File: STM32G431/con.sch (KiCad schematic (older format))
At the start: 61 parts, among them J10 NTC, J11 LED, J4 GND, J5 VIN, J6 UART, J8 HALL, J9 AIN/PWM, P1 TC2030-CTX-Tag-Connect, Q2 Q_NMOS_GSD, U11 USBLC6-4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

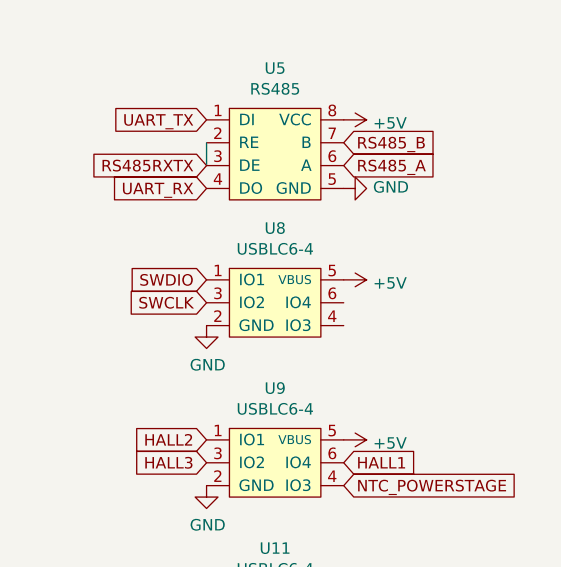
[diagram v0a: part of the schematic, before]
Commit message: updated layout
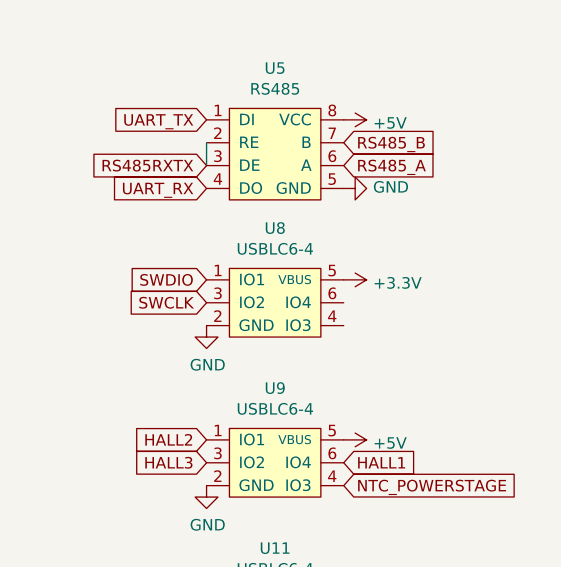
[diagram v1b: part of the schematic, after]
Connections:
- net +3V3: now also U8.5 (VBUS)
- net +5V: no longer U8.5 (VBUS)
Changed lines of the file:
@@
-	0    1    1    0
-$EndComp
-$Comp
-L power:+5V #PWR0171
-U 1 1 5CEAAB05
-P 10150 3400
-F 0 "#PWR0171" H 10150 3250 50  0001 C CNN
-F 1 "+5V" V 10165 3528 50  0000 L CNN
-F 2 "" H 10150 3400 50  0001 C CNN
-F 3 "" H 10150 3400 50  0001 C CNN
-	1    10150 3400
 	0    1    1    0
 $EndComp
@@
 Text Label 7650 1100 0    50   ~ 0
 AinC
+$Comp
+L power:+3.3V #PWR?
+U 1 1 5E15C1C9
+P 10150 3400
+F 0 "#PWR?" H 10150 3250 50  0001 C CNN
+F 1 "+3.3V" V 10165 3528 50  0000 L CNN
+F 2 "" H 10150 3400 50  0001 C CNN
+F 3 "" H 10150 3400 50  0001 C CNN
+	1    10150 3400
+	0    1    1    0
+$EndComp
 $EndSCHEMATC

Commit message: updated layout
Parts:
- R27, R28, R29, R33, R34, R35: footprint Resistor_SMD:R_0402_1005Metric -> Resistor_SMD:R_0603_1608Metric
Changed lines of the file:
@@
 F 0 "R35" H 6458 1704 50  0000 L CNN
 F 1 "10k" H 6458 1795 50  0000 L CNN
-F 2 "Resistor_SMD:R_0402_1005Metric" H 6400 1750 50  0001 C CNN
+F 2 "Resistor_SMD:R_0603_1608Metric" H 6400 1750 50  0001 C CNN
 F 3 "~" H 6400 1750 50  0001 C CNN
 	1    6400 1750
@@
 F 0 "R34" H 6600 2100 50  0000 R CNN
 F 1 "10k" H 6550 1950 50  0000 R CNN
-F 2 "Resistor_SMD:R_0402_1005Metric" H 6500 1750 50  0001 C CNN
+F 2 "Resistor_SMD:R_0603_1608Metric" H 6500 1750 50  0001 C CNN
 F 3 "~" H 6500 1750 50  0001 C CNN
 	1    6500 1750
@@
 F 0 "R33" H 6541 1704 50  0000 R CNN
 F 1 "10k" H 6541 1795 50  0000 R CNN
-F 2 "Resistor_SMD:R_0402_1005Metric" H 6600 1750 50  0001 C CNN
+F 2 "Resistor_SMD:R_0603_1608Metric" H 6600 1750 50  0001 C CNN
 F 3 "~" H 6600 1750 50  0001 C CNN
 	1    6600 1750
@@
 F 0 "R28" V 6200 750 50  0000 C CNN
 F 1 "1.8k" V 6300 750 50  0000 C CNN
-F 2 "Resistor_SMD:R_0402_1005Metric" H 6250 1200 50  0001 C CNN
+F 2 "Resistor_SMD:R_0603_1608Metric" H 6250 1200 50  0001 C CNN
 F 3 "~" H 6250 1200 50  0001 C CNN
 	1    6250 1200
@@
 F 0 "R27" V 6054 1100 50  0000 C CNN
 F 1 "1.8k" V 6145 1100 50  0000 C CNN
-F 2 "Resistor_SMD:R_0402_1005Metric" H 6250 1100 50  0001 C CNN
+F 2 "Resistor_SMD:R_0603_1608Metric" H 6250 1100 50  0001 C CNN
 F 3 "~" H 6250 1100 50  0001 C CNN
 	1    6250 1100
@@
 F 0 "R29" V 6354 1300 50  0000 C CNN
 F 1 "1.8k" V 6445 1300 50  0000 C CNN
-F 2 "Resistor_SMD:R_0402_1005Metric" H 6250 1300 50  0001 C CNN
+F 2 "Resistor_SMD:R_0603_1608Metric" H 6250 1300 50  0001 C CNN
 F 3 "~" H 6250 1300 50  0001 C CNN
 	1    6250 1300

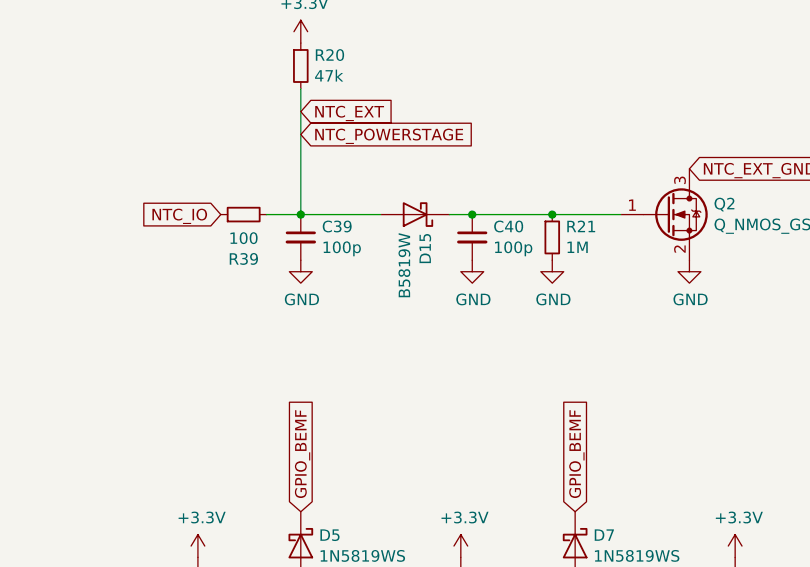
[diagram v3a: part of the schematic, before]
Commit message: updated layout
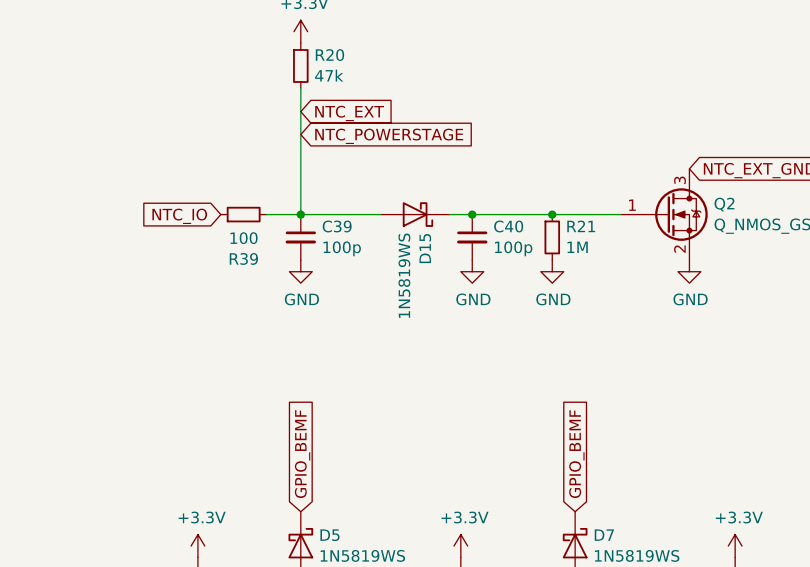
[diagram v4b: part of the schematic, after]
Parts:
- D15: value B5819W -> 1N5819WS; footprint Diode_SMD:D_SOD-123 -> Diode_SMD:D_SOD-323
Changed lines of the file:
@@
 P 4650 5200
 F 0 "D15" V 4604 5279 50  0000 L CNN
-F 1 "B5819W" V 4695 5279 50  0000 L CNN
-F 2 "Diode_SMD:D_SOD-123" H 4650 5200 50  0001 C CNN
+F 1 "1N5819WS" V 4695 5279 50  0000 L CNN
+F 2 "Diode_SMD:D_SOD-323" H 4650 5200 50  0001 C CNN
 F 3 "https://datasheet.lcsc.com/szlcsc/Changjiang-Electronics-Tech-CJ-B5819W_C8598.pdf" H 4650 5200 50  0001 C CNN
 F 4 "C8598" H 4650 5200 50  0001 C CNN "LCSC"

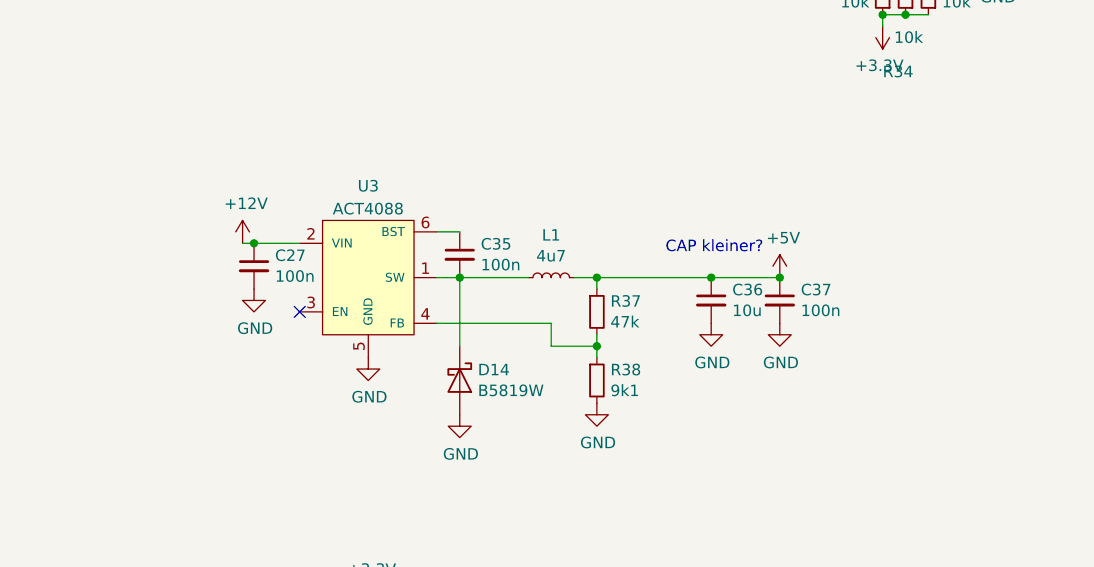
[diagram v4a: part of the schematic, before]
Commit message: updated layout
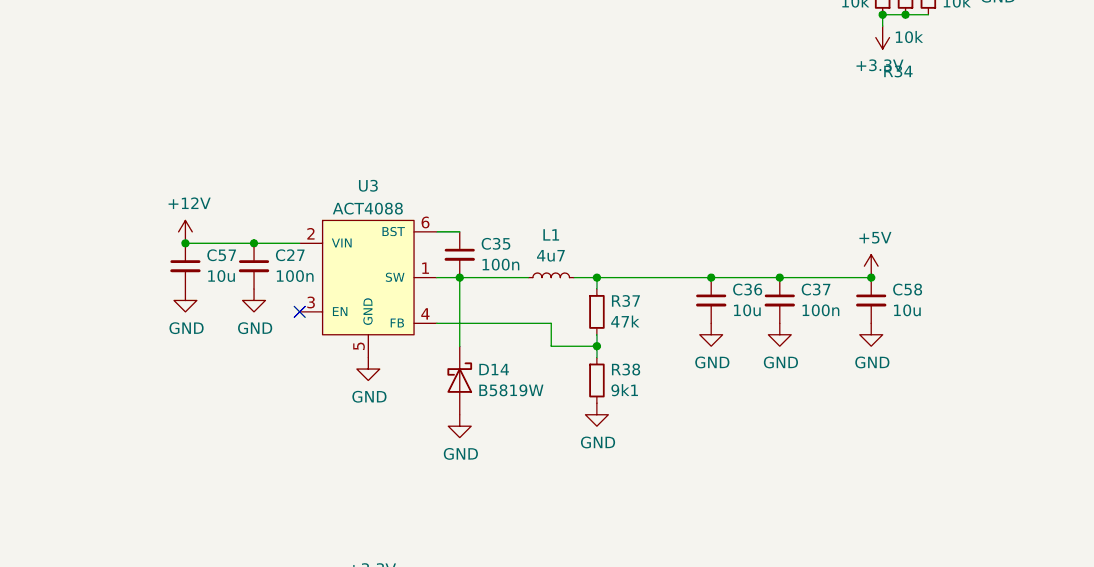
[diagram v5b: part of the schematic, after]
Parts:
- added C57, C58: 10u, Capacitor_SMD:C_1206_3216Metric, symbol Device:C_Small
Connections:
- net +12V: now also C57.1
- net +5V: now also C58.1
- net GND: now also C57.2, C58.2
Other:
- note removed: "CAP kleiner?"
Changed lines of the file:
@@
 L power:+5V #PWR0150
 U 1 1 5CEAAA14
-P 5950 3000
-F 0 "#PWR0150" H 5950 2850 50  0001 C CNN
-F 1 "+5V" H 5965 3173 50  0000 C CNN
-F 2 "" H 5950 3000 50  0001 C CNN
-F 3 "" H 5950 3000 50  0001 C CNN
-	1    5950 3000
+P 6350 3000
+F 0 "#PWR0150" H 6350 2850 50  0001 C CNN
+F 1 "+5V" H 6365 3173 50  0000 C CNN
+F 2 "" H 6350 3000 50  0001 C CNN
+F 3 "" H 6350 3000 50  0001 C CNN
+	1    6350 3000
 	1    0    0    -1
 $EndComp
@@
 	3650 2850 3850 2850
 Connection ~ 3650 2850
-Wire Wire Line
-	3600 2850 3650 2850
 $Comp
 L Device:C_Small C27
@@
 	1    0    0    -1
 $EndComp
-Text Notes 5450 2900 0    50   ~ 0
-CAP kleiner?
 Text GLabel 2750 7150 2    50   Input ~ 0
 SWCLK
@@
 L power:+12V #PWR0217
 U 1 1 5DED744B
-P 3600 2850
-F 0 "#PWR0217" H 3600 2700 50  0001 C CNN
-F 1 "+12V" H 3615 3023 50  0000 C CNN
-F 2 "" H 3600 2850 50  0001 C CNN
-F 3 "" H 3600 2850 50  0001 C CNN
-	1    3600 2850
+P 3350 2850
+F 0 "#PWR0217" H 3350 2700 50  0001 C CNN
+F 1 "+12V" H 3365 3023 50  0000 C CNN
+F 2 "" H 3350 2850 50  0001 C CNN
+F 3 "" H 3350 2850 50  0001 C CNN
+	1    3350 2850
 	1    0    0    -1
 $EndComp
@@
 	0    1    1    0
 $EndComp
+$Comp
+L power:GND #PWR0234
+U 1 1 5DF96379
+P 6350 3200
+F 0 "#PWR0234" H 6350 2950 50  0001 C CNN
+F 1 "GND" H 6355 3027 50  0000 C CNN
+F 2 "" H 6350 3200 50  0001 C CNN
+F 3 "" H 6350 3200 50  0001 C CNN
+	1    6350 3200
+	1    0    0    -1
+$EndComp
+$Comp
+L Device:C_Small C58
+U 1 1 5DF9637F
+P 6350 3100
+F 0 "C58" H 6442 3146 50  0000 L CNN
+F 1 "10u" H 6442 3055 50  0000 L CNN
+F 2 "Capacitor_SMD:C_1206_3216Metric" H 6350 3100 50  0001 C CNN
+F 3 "~" H 6350 3100 50  0001 C CNN
+	1    6350 3100
+	1    0    0    -1
+$EndComp
+$Comp
+L power:GND #PWR0235
+U 1 1 5DF98EE3
+P 3350 3050
+F 0 "#PWR0235" H 3350 2800 50  0001 C CNN
+F 1 "GND" H 3355 2877 50  0000 C CNN
+F 2 "" H 3350 3050 50  0001 C CNN
+F 3 "" H 3350 3050 50  0001 C CNN
+	1    3350 3050
+	1    0    0    -1
+$EndComp
+$Comp
+L Device:C_Small C57
+U 1 1 5DF98EE9
+P 3350 2950
+F 0 "C57" H 3442 2996 50  0000 L CNN
+F 1 "10u" H 3442 2905 50  0000 L CNN
+F 2 "Capacitor_SMD:C_1206_3216Metric" H 3350 2950 50  0001 C CNN
+F 3 "~" H 3350 2950 50  0001 C CNN
+	1    3350 2950
+	1    0    0    -1
+$EndComp
+Wire Wire Line
+	3350 2850 3650 2850
+Connection ~ 3350 2850
+Wire Wire Line
+	6350 3000 5950 3000
+Connection ~ 6350 3000
 $EndSCHEMATC

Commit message: updated layout
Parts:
- R17, R6: footprint Capacitor_SMD:C_0402_1005Metric -> Resistor_SMD:R_0402_1005Metric
- R23, R25, R30: footprint Resistor_SMD:R_0402_1005Metric -> Resistor_SMD:R_0603_1608Metric
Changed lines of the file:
@@
 F 0 "R30" V 6546 7050 50  0000 C CNN
 F 1 "100k" V 6455 7050 50  0000 C CNN
-F 2 "Resistor_SMD:R_0402_1005Metric" H 6650 7050 50  0001 C CNN
+F 2 "Resistor_SMD:R_0603_1608Metric" H 6650 7050 50  0001 C CNN
 F 3 "~" H 6650 7050 50  0001 C CNN
 	1    6650 7050
@@
 F 0 "R25" V 5604 7050 50  0000 C CNN
 F 1 "100k" V 5695 7050 50  0000 C CNN
-F 2 "Resistor_SMD:R_0402_1005Metric" H 5500 7050 50  0001 C CNN
+F 2 "Resistor_SMD:R_0603_1608Metric" H 5500 7050 50  0001 C CNN
 F 3 "~" H 5500 7050 50  0001 C CNN
 	1    5500 7050
@@
 F 0 "R23" V 4404 7050 50  0000 C CNN
 F 1 "100k" V 4495 7050 50  0000 C CNN
-F 2 "Resistor_SMD:R_0402_1005Metric" H 4300 7050 50  0001 C CNN
+F 2 "Resistor_SMD:R_0603_1608Metric" H 4300 7050 50  0001 C CNN
 F 3 "~" H 4300 7050 50  0001 C CNN
 	1    4300 7050
@@
 F 0 "R6" H 7809 5896 50  0000 L CNN
 F 1 "100k" H 7809 5805 50  0000 L CNN
-F 2 "Capacitor_SMD:C_0402_1005Metric" H 7750 5850 50  0001 C CNN
+F 2 "Resistor_SMD:R_0402_1005Metric" H 7750 5850 50  0001 C CNN
 F 3 "~" H 7750 5850 50  0001 C CNN
 	1    7750 5850
@@
 F 0 "R17" H 7809 6196 50  0000 L CNN
 F 1 "4k3" H 7809 6105 50  0000 L CNN
-F 2 "Capacitor_SMD:C_0402_1005Metric" H 7750 6150 50  0001 C CNN
+F 2 "Resistor_SMD:R_0402_1005Metric" H 7750 6150 50  0001 C CNN
 F 3 "~" H 7750 6150 50  0001 C CNN
 	1    7750 6150

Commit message: updated files
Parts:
- C29, C30, C31: value 100p -> DNP
- C39, C40: footprint Resistor_SMD:R_0402_1005Metric -> Capacitor_SMD:C_0402_1005Metric
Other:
- moved on the sheet: C42, R17, R6
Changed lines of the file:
@@
 EESchema Schematic File Version 4
-LIBS:STM32G431-cache
 EELAYER 30 0
 EELAYER END
@@
 AR Path="/5D59ABFE/5D5B749F" Ref="C31"  Part="1"
 F 0 "C31" H 6092 7246 50  0000 L CNN
-F 1 "100p" H 6092 7155 50  0000 L CNN
+F 1 "DNP" H 6092 7155 50  0000 L CNN
 F 2 "Capacitor_SMD:C_0402_1005Metric" H 6000 7200 50  0001 C CNN
 F 3 "~" H 6000 7200 50  0001 C CNN
@@
 AR Path="/5D59ABFE/5D5B74C4" Ref="C30"  Part="1"
 F 0 "C30" H 4892 7246 50  0000 L CNN
-F 1 "100p" H 4892 7155 50  0000 L CNN
+F 1 "DNP" H 4892 7155 50  0000 L CNN
 F 2 "Capacitor_SMD:C_0402_1005Metric" H 4800 7200 50  0001 C CNN
 F 3 "~" H 4800 7200 50  0001 C CNN
@@
 AR Path="/5D59ABFE/5D5B74E9" Ref="C29"  Part="1"
 F 0 "C29" H 3742 7246 50  0000 L CNN
-F 1 "100p" H 3742 7155 50  0000 L CNN
+F 1 "DNP" H 3742 7155 50  0000 L CNN
 F 2 "Capacitor_SMD:C_0402_1005Metric" H 3650 7200 50  0001 C CNN
 F 3 "~" H 3650 7200 50  0001 C CNN
@@
 F 0 "C39" H 4242 5346 50  0000 L CNN
 F 1 "100p" H 4242 5255 50  0000 L CNN
-F 2 "Resistor_SMD:R_0402_1005Metric" H 4150 5300 50  0001 C CNN
+F 2 "Capacitor_SMD:C_0402_1005Metric" H 4150 5300 50  0001 C CNN
 F 3 "~" H 4150 5300 50  0001 C CNN
 	1    4150 5300
@@
 F 0 "C40" H 4992 5346 50  0000 L CNN
 F 1 "100p" H 4992 5255 50  0000 L CNN
-F 2 "Resistor_SMD:R_0402_1005Metric" H 4900 5300 50  0001 C CNN
+F 2 "Capacitor_SMD:C_0402_1005Metric" H 4900 5300 50  0001 C CNN
 F 3 "~" H 4900 5300 50  0001 C CNN
 	1    4900 5300
@@
 Connection ~ 5250 5200
 $Comp
-L Device:Q_NMOS_GSD Q2
-U 1 1 5CDECFF4
-P 5750 5200
-F 0 "Q2" H 5956 5246 50  0000 L CNN
-F 1 "Q_NMOS_GSD" H 5956 5155 50  0000 L CNN
-F 2 "Package_TO_SOT_SMD:SOT-23" H 5950 5300 50  0001 C CNN
-F 3 "~" H 5750 5200 50  0001 C CNN
-	1    5750 5200
-	1    0    0    -1
-$EndComp
-$Comp
 L power:GND #PWR0181
 U 1 1 5CDEE814
@@
 	1    0    0    -1
 $EndComp
-Text GLabel 5850 5000 2    50   Input ~ 0
+Text GLabel 5850 5000 1    50   Input ~ 0
 NTC_EXT_GND
 Text GLabel 8900 1000 0    50   Input ~ 0
@@
 L Device:R_Small R?
 U 1 1 5CEAA519
-P 7750 5850
+P 7850 4050
 AR Path="/5CEAA519" Ref="R?"  Part="1"
 AR Path="/5D59ABFE/5CEAA519" Ref="R6"  Part="1"
-F 0 "R6" H 7809 5896 50  0000 L CNN
-F 1 "100k" H 7809 5805 50  0000 L CNN
-F 2 "Resistor_SMD:R_0402_1005Metric" H 7750 5850 50  0001 C CNN
-F 3 "~" H 7750 5850 50  0001 C CNN
-	1    7750 5850
+F 0 "R6" H 7909 4096 50  0000 L CNN
+F 1 "100k" H 7909 4005 50  0000 L CNN
+F 2 "Resistor_SMD:R_0402_1005Metric" H 7850 4050 50  0001 C CNN
+F 3 "~" H 7850 4050 50  0001 C CNN
+	1    7850 4050
 	1    0    0    -1
 $EndComp
@@
 L Device:R_Small R?
 U 1 1 5CEAA51F
-P 7750 6150
+P 7850 4350
 AR Path="/5CEAA51F" Ref="R?"  Part="1"
 AR Path="/5D59ABFE/5CEAA51F" Ref="R17"  Part="1"
-F 0 "R17" H 7809 6196 50  0000 L CNN
-F 1 "4k3" H 7809 6105 50  0000 L CNN
-F 2 "Resistor_SMD:R_0402_1005Metric" H 7750 6150 50  0001 C CNN
-F 3 "~" H 7750 6150 50  0001 C CNN
-	1    7750 6150
+F 0 "R17" H 7909 4396 50  0000 L CNN
+F 1 "4k3" H 7909 4305 50  0000 L CNN
+F 2 "Resistor_SMD:R_0402_1005Metric" H 7850 4350 50  0001 C CNN
+F 3 "~" H 7850 4350 50  0001 C CNN
+	1    7850 4350
 	1    0    0    -1
 $EndComp
@@
 L Device:C_Small C?
 U 1 1 5CEAA525
-P 7450 6150
+P 7550 4350
 AR Path="/5CEAA525" Ref="C?"  Part="1"
 AR Path="/5D59ABFE/5CEAA525" Ref="C42"  Part="1"
-F 0 "C42" H 7542 6196 50  0000 L CNN
-F 1 "100p" H 7542 6105 50  0000 L CNN
-F 2 "Capacitor_SMD:C_0402_1005Metric" H 7450 6150 50  0001 C CNN
-F 3 "~" H 7450 6150 50  0001 C CNN
-	1    7450 6150
+F 0 "C42" H 7642 4396 50  0000 L CNN
+F 1 "100p" H 7642 4305 50  0000 L CNN
+F 2 "Capacitor_SMD:C_0402_1005Metric" H 7550 4350 50  0001 C CNN
+F 3 "~" H 7550 4350 50  0001 C CNN
+	1    7550 4350
 	1    0    0    -1
 $EndComp
@@
 L power:GND #PWR?
 U 1 1 5CEAA52B
-P 7750 6250
+P 7850 4450
 AR Path="/5CEAA52B" Ref="#PWR?"  Part="1"
 AR Path="/5D59ABFE/5CEAA52B" Ref="#PWR0191"  Part="1"
-F 0 "#PWR0191" H 7750 6000 50  0001 C CNN
-F 1 "GND" H 7755 6077 50  0000 C CNN
-F 2 "" H 7750 6250 50  0001 C CNN
-F 3 "" H 7750 6250 50  0001 C CNN
-	1    7750 6250
+F 0 "#PWR0191" H 7850 4200 50  0001 C CNN
+F 1 "GND" H 7855 4277 50  0000 C CNN
+F 2 "" H 7850 4450 50  0001 C CNN
+F 3 "" H 7850 4450 50  0001 C CNN
+	1    7850 4450
 	1    0    0    -1
 $EndComp
@@
 L power:GND #PWR?
 U 1 1 5CEAA531
-P 7450 6250
+P 7550 4450
 AR Path="/5CEAA531" Ref="#PWR?"  Part="1"
 AR Path="/5D59ABFE/5CEAA531" Ref="#PWR0192"  Part="1"
-F 0 "#PWR0192" H 7450 6000 50  0001 C CNN
-F 1 "GND" H 7455 6077 50  0000 C CNN
-F 2 "" H 7450 6250 50  0001 C CNN
-F 3 "" H 7450 6250 50  0001 C CNN
-	1    7450 6250
-	1    0    0    -1
-$EndComp
-Wire Wire Line
-	7750 5950 7750 6000
-Wire Wire Line
-	7750 6000 7450 6000
-Wire Wire Line
-	7450 6000 7450 6050
-Connection ~ 7750 6000
-Wire Wire Line
-	7750 6000 7750 6050
-Text GLabel 7450 6000 0    50   Input ~ 0
+F 0 "#PWR0192" H 7550 4200 50  0001 C CNN
+F 1 "GND" H 7555 4277 50  0000 C CNN
+F 2 "" H 7550 4450 50  0001 C CNN
+F 3 "" H 7550 4450 50  0001 C CNN
+	1    7550 4450
+	1    0    0    -1
+$EndComp
+Wire Wire Line
+	7850 4150 7850 4200
+Wire Wire Line
+	7850 4200 7550 4200
+Wire Wire Line
+	7550 4200 7550 4250
+Connection ~ 7850 4200
+Wire Wire Line
+	7850 4200 7850 4250
+Text GLabel 7550 4200 0    50   Input ~ 0
 Vin_mon
-Text GLabel 7750 5750 1    50   Input ~ 0
+Text GLabel 7850 3950 1    50   Input ~ 0
 VIN
 $Comp
@@
 P 4850 850
 F 0 "#PWR0213" H 4850 700 50  0001 C CNN
-F 1 "+3.3V" H 4865 1023 50  0000 C CNN
+F 1 "+3.3V" V 4983 887 50  0000 C CNN
 F 2 "" H 4850 850 50  0001 C CNN
 F 3 "" H 4850 850 50  0001 C CNN
@@
 P 7850 900
 F 0 "#PWR0214" H 7850 750 50  0001 C CNN
-F 1 "+3.3V" H 7865 1073 50  0000 C CNN
+F 1 "+3.3V" V 7865 1028 50  0000 L CNN
 F 2 "" H 7850 900 50  0001 C CNN
 F 3 "" H 7850 900 50  0001 C CNN
@@
 	6350 3000 5950 3000
 Connection ~ 6350 3000
+$Comp
+L Device:Q_NMOS_GSD Q2
+U 1 1 5CDECFF4
+P 5750 5200
+F 0 "Q2" H 5956 5246 50  0000 L CNN
+F 1 "Q_NMOS_GSD" H 5956 5155 50  0000 L CNN
+F 2 "Package_TO_SOT_SMD:SOT-23" H 5950 5300 50  0001 C CNN
+F 3 "~" H 5750 5200 50  0001 C CNN
+	1    5750 5200
+	1    0    0    -1
+$EndComp
 $EndSCHEMATC
